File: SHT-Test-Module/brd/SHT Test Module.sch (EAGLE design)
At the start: 13 parts

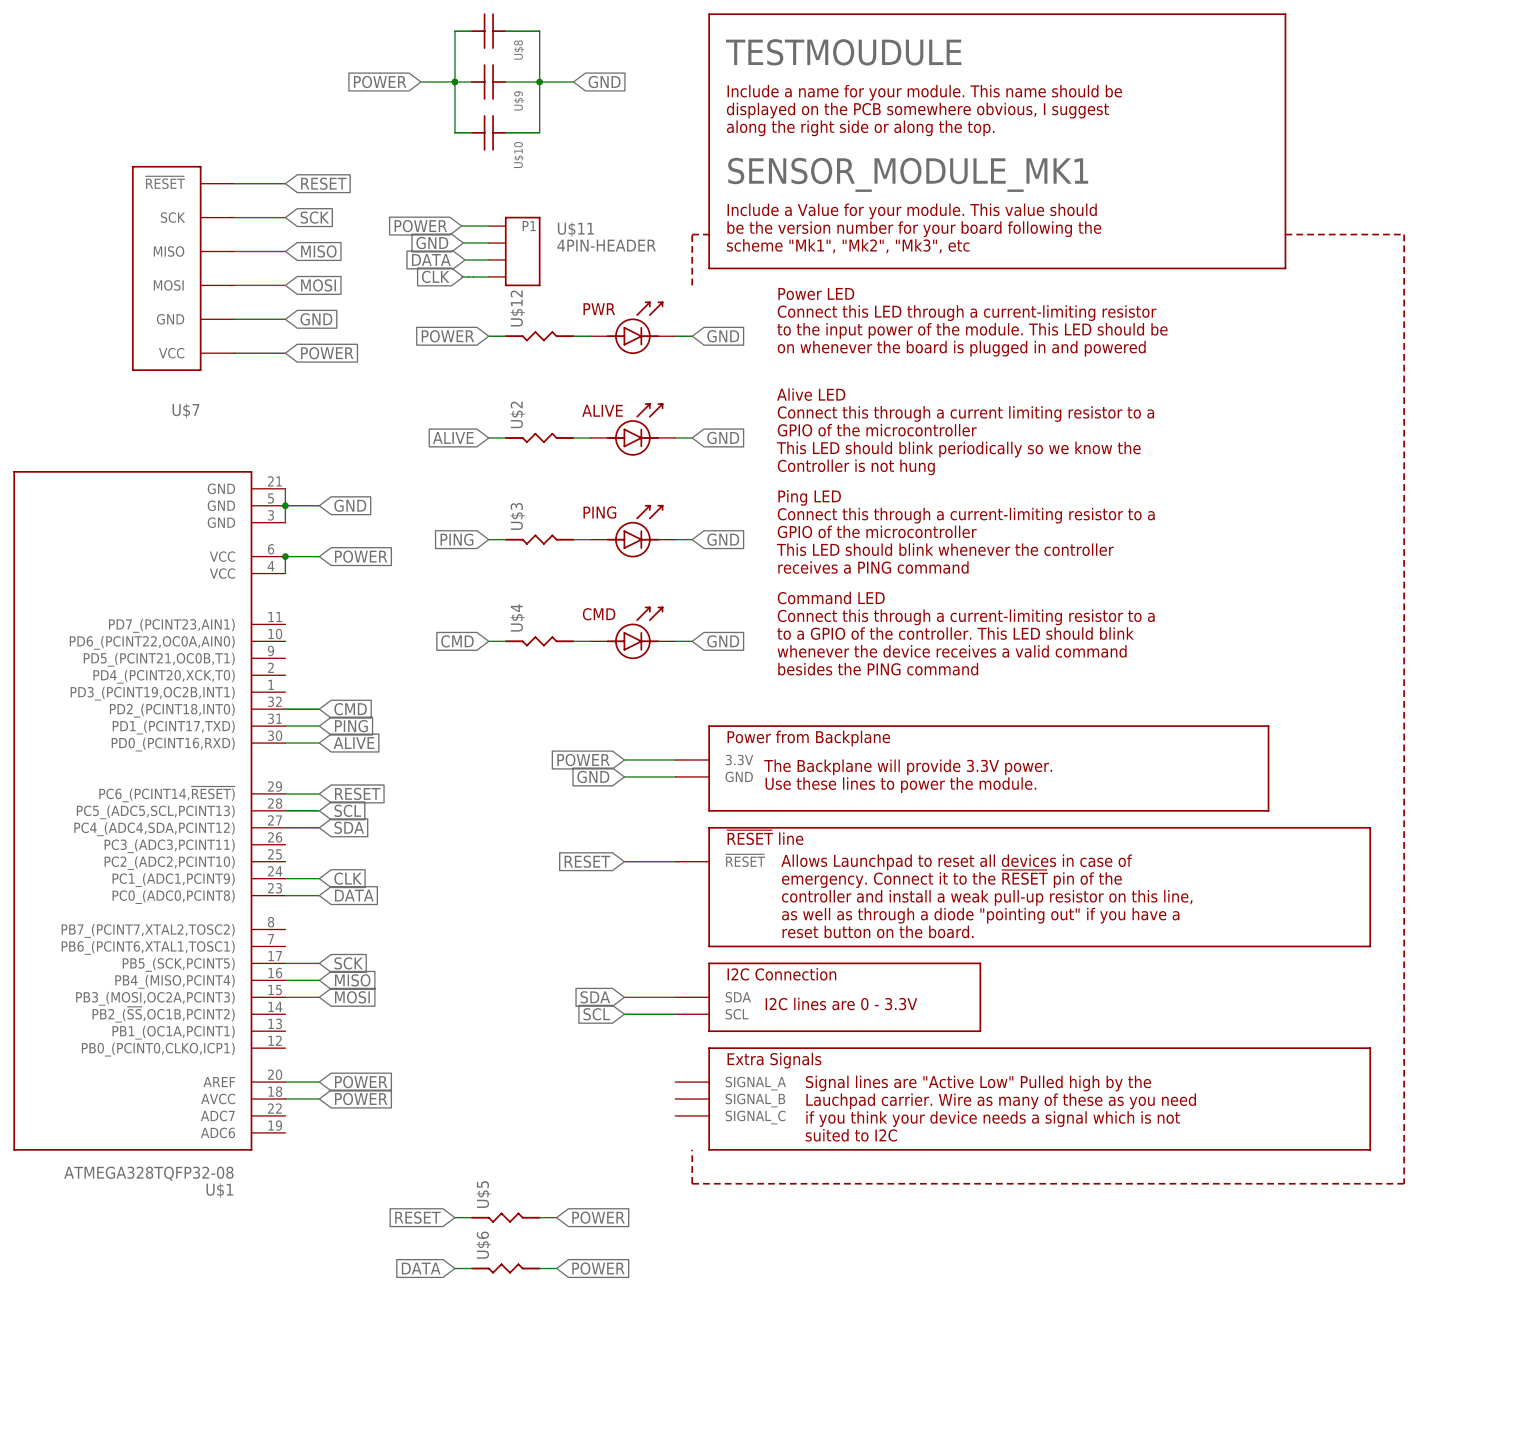
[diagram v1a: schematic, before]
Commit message: updated board templates and modified existing boards to use the mk2 templates.
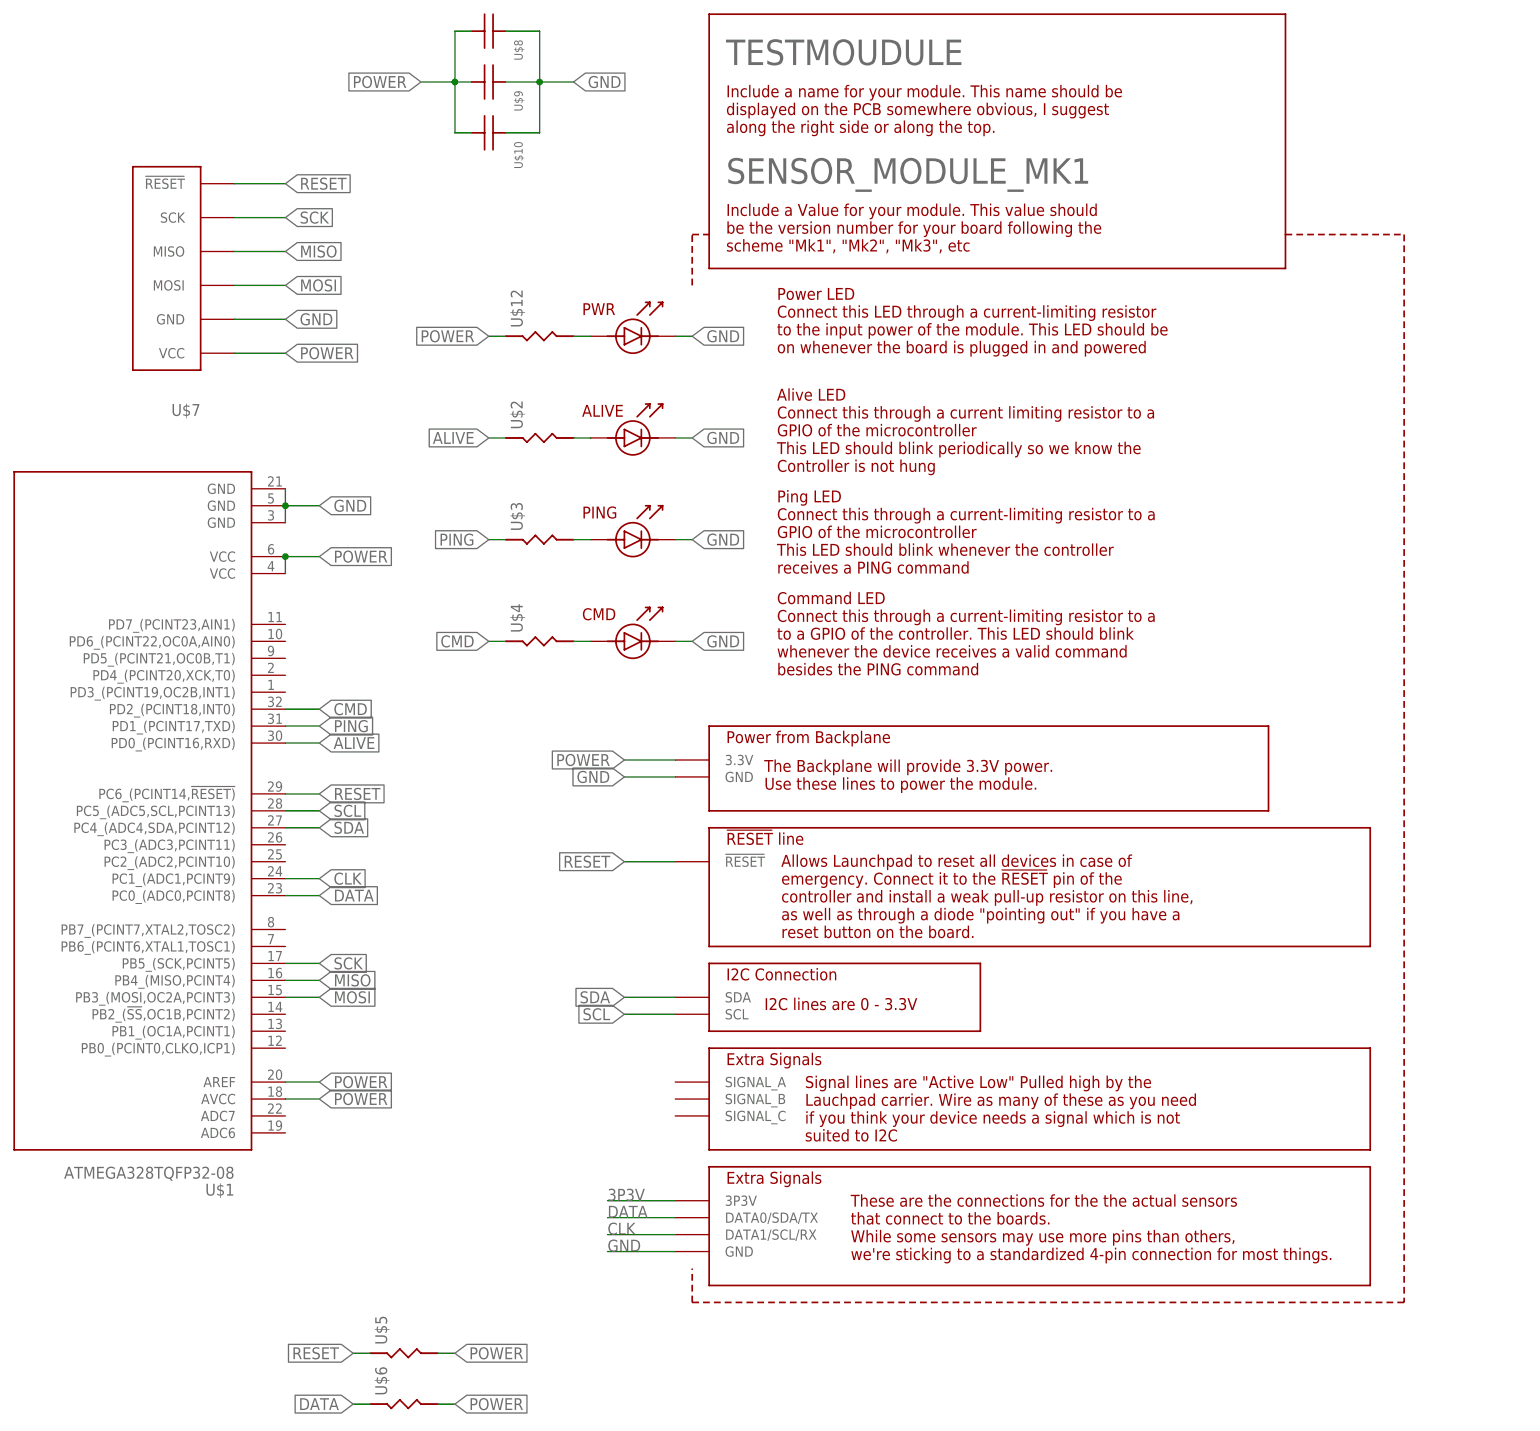
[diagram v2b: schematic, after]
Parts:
- removed U$11: 4PIN-HEADER, 000_CustomPartsMaster:4PIN-HEADER
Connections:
- new net 3P3V: TESTMOUDULE.3P3V
- net CLK: now also TESTMOUDULE.DATA1/SCL/RX; no longer U$11.P$4
- net DATA: now also TESTMOUDULE.DATA0/SDA/TX; no longer U$11.P$3
- net GND: now also TESTMOUDULE.GND@1, TESTMOUDULE.GND@2; no longer TESTMOUDULE.GND, U$11.P$2
- net POWER: no longer U$11.P1
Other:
- moved on the sheet: U$5, U$6
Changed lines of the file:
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@@
 <layers>
 <layer number="1" name="Top" color="4" fill="1" visible="no" active="no"/>
+<layer number="2" name="Route2" color="1" fill="3" visible="no" active="no"/>
+<layer number="15" name="Route15" color="4" fill="6" visible="no" active="no"/>
 <layer number="16" name="Bottom" color="1" fill="1" visible="no" active="no"/>
 <layer number="17" name="Pads" color="2" fill="1" visible="no" active="no"/>
@@
 <part name="U$9" library="000_CustomPartsMaster" deviceset="CAPACITOR-UNPOLARIZED" device="0805"/>
 <part name="U$10" library="000_CustomPartsMaster" deviceset="CAPACITOR-UNPOLARIZED" device="0805"/>
-<part name="U$11" library="000_CustomPartsMaster" deviceset="4PIN-HEADER" device=""/>
 <part name="U$12" library="000_CustomPartsMaster" deviceset="RESISTOR" device=""/>
 </parts>
@@
 <instance part="U$3" gate="G$1" x="99.06" y="96.52" rot="R90"/>
 <instance part="U$4" gate="G$1" x="99.06" y="81.28" rot="R90"/>
-<instance part="U$5" gate="G$1" x="93.98" y="-5.08" rot="R90"/>
-<instance part="U$6" gate="G$1" x="93.98" y="-12.7" rot="R90"/>
+<instance part="U$5" gate="G$1" x="78.74" y="-25.4" rot="R90"/>
+<instance part="U$6" gate="G$1" x="78.74" y="-33.02" rot="R90"/>
 <instance part="U$7" gate="G$1" x="48.26" y="137.16" rot="R180"/>
 <instance part="U$8" gate="G$1" x="91.44" y="172.72" rot="R270"/>
 <instance part="U$9" gate="G$1" x="91.44" y="165.1" rot="R270"/>
 <instance part="U$10" gate="G$1" x="91.44" y="157.48" rot="R270"/>
-<instance part="U$11" gate="G$1" x="93.98" y="139.7"/>
 <instance part="U$12" gate="G$1" x="99.06" y="127" rot="R90"/>
 </instances>
@@
 <segment>
 <pinref part="U$5" gate="G$1" pin="P$2"/>
-<wire x1="99.06" y1="-5.08" x2="101.6" y2="-5.08" width="0.1524" layer="91"/>
-<label x="101.6" y="-5.08" size="1.778" layer="95" xref="yes"/>
+<wire x1="83.82" y1="-25.4" x2="86.36" y2="-25.4" width="0.1524" layer="91"/>
+<label x="86.36" y="-25.4" size="1.778" layer="95" xref="yes"/>
 </segment>
 <segment>
 <pinref part="U$6" gate="G$1" pin="P$2"/>
-<wire x1="99.06" y1="-12.7" x2="101.6" y2="-12.7" width="0.1524" layer="91"/>
-<label x="101.6" y="-12.7" size="1.778" layer="95" xref="yes"/>
+<wire x1="83.82" y1="-33.02" x2="86.36" y2="-33.02" width="0.1524" layer="91"/>
+<label x="86.36" y="-33.02" size="1.778" layer="95" xref="yes"/>
 </segment>
 <segment>
@@
 <label x="91.44" y="127" size="1.778" layer="95" rot="R180" xref="yes"/>
 </segment>
-<segment>
-<pinref part="U$11" gate="G$1" pin="P1"/>
-<wire x1="91.44" y1="143.51" x2="87.376" y2="143.51" width="0.1524" layer="91"/>
-<label x="87.376" y="143.51" size="1.778" layer="95" rot="R180" xref="yes"/>
-</segment>
 </net>
 <net name="GND" class="0">
@@
 </segment>
 <segment>
-<pinref part="TESTMOUDULE" gate="G$1" pin="GND"/>
+<pinref part="TESTMOUDULE" gate="G$1" pin="GND@1"/>
 <wire x1="119.38" y1="60.96" x2="111.76" y2="60.96" width="0.1524" layer="91"/>
 <label x="111.76" y="60.96" size="1.778" layer="95" rot="R180" xref="yes"/>
@@
 </segment>
 <segment>
-<pinref part="U$11" gate="G$1" pin="P$2"/>
-<wire x1="91.44" y1="140.97" x2="87.63" y2="140.97" width="0.1524" layer="91"/>
-<label x="87.63" y="140.97" size="1.778" layer="95" rot="R180" xref="yes"/>
+<pinref part="TESTMOUDULE" gate="G$1" pin="GND@2"/>
+<wire x1="119.38" y1="-10.16" x2="109.22" y2="-10.16" width="0.1524" layer="91"/>
+<label x="109.22" y="-10.16" size="1.778" layer="95"/>
 </segment>
 </net>
@@
 <segment>
 <pinref part="U$5" gate="G$1" pin="P$1"/>
-<wire x1="88.9" y1="-5.08" x2="86.36" y2="-5.08" width="0.1524" layer="91"/>
-<label x="86.36" y="-5.08" size="1.778" layer="95" rot="R180" xref="yes"/>
+<wire x1="73.66" y1="-25.4" x2="71.12" y2="-25.4" width="0.1524" layer="91"/>
+<label x="71.12" y="-25.4" size="1.778" layer="95" rot="R180" xref="yes"/>
 </segment>
 <segment>
@@
 <segment>
 <pinref part="U$6" gate="G$1" pin="P$1"/>
-<wire x1="88.9" y1="-12.7" x2="86.36" y2="-12.7" width="0.1524" layer="91"/>
-<label x="86.36" y="-12.7" size="1.778" layer="95" rot="R180" xref="yes"/>
-</segment>
-<segment>
-<pinref part="U$11" gate="G$1" pin="P$3"/>
-<wire x1="91.44" y1="138.43" x2="87.884" y2="138.43" width="0.1524" layer="91"/>
-<label x="87.884" y="138.43" size="1.778" layer="95" rot="R180" xref="yes"/>
+<wire x1="73.66" y1="-33.02" x2="71.12" y2="-33.02" width="0.1524" layer="91"/>
+<label x="71.12" y="-33.02" size="1.778" layer="95" rot="R180" xref="yes"/>
+</segment>
+<segment>
+<pinref part="TESTMOUDULE" gate="G$1" pin="DATA0/SDA/TX"/>
+<wire x1="119.38" y1="-5.08" x2="109.22" y2="-5.08" width="0.1524" layer="91"/>
+<label x="109.22" y="-5.08" size="1.778" layer="95"/>
 </segment>
 </net>
@@
 </segment>
 <segment>
-<pinref part="U$11" gate="G$1" pin="P$4"/>
-<wire x1="91.44" y1="135.89" x2="89.154" y2="135.89" width="0.1524" layer="91"/>
-<wire x1="89.154" y1="135.89" x2="88.392" y2="135.89" width="0.1524" layer="91"/>
-<wire x1="87.376" y1="135.89" x2="88.392" y2="135.89" width="0.1524" layer="91"/>
-<label x="87.63" y="135.89" size="1.778" layer="95" rot="R180" xref="yes"/>
+<pinref part="TESTMOUDULE" gate="G$1" pin="DATA1/SCL/RX"/>
+<wire x1="119.38" y1="-7.62" x2="109.22" y2="-7.62" width="0.1524" layer="91"/>
+<label x="109.22" y="-7.62" size="1.778" layer="95"/>
 </segment>
 </net>
@@
 </segment>
 </net>
+<net name="3P3V" class="0">
+<segment>
+<pinref part="TESTMOUDULE" gate="G$1" pin="3P3V"/>
+<wire x1="119.38" y1="-2.54" x2="109.22" y2="-2.54" width="0.1524" layer="91"/>
+<label x="109.22" y="-2.54" size="1.778" layer="95"/>
+</segment>
+</net>
